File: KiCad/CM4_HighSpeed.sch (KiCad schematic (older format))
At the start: 6 parts

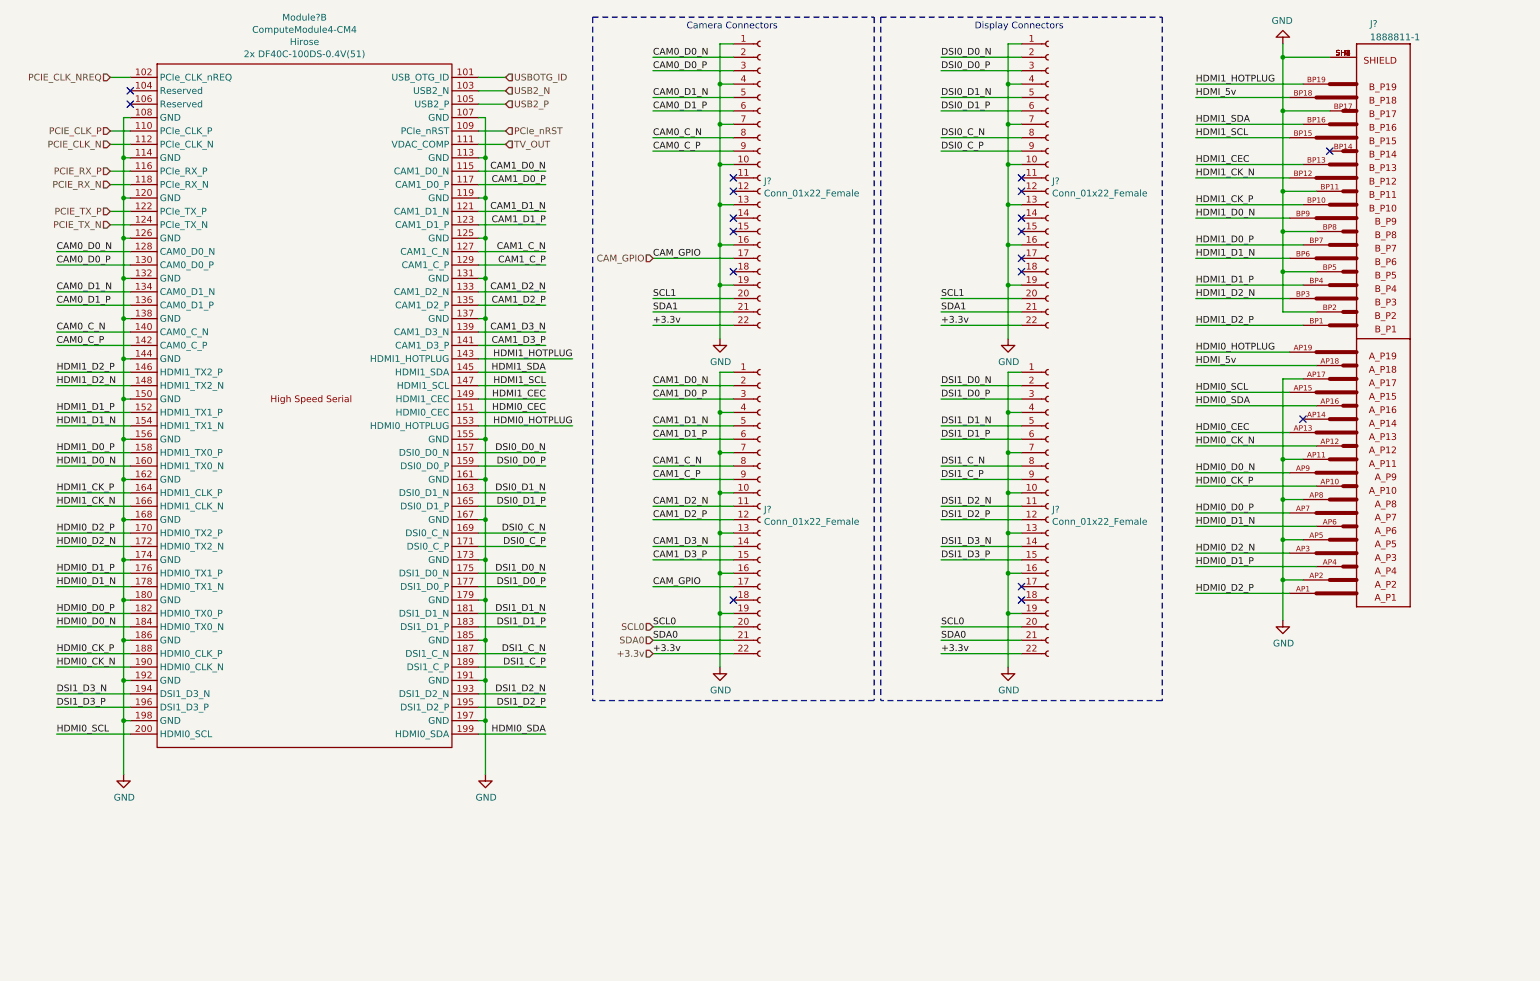
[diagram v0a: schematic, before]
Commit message: Lotsa changes
Added new footprints:
PCIe x1, TO-252 tab, SOT95, SOP50, SON50, Hirose FH-12-22S, 2.54mm 2x02 and 2x05 headers
Added new models:
Hirose FH-12-22S, FSUSB42MUX, MIC2019YM6-TR, TPS6206
Re-did ATX connector symbol wiring
Begun wiring PI7C PCI-e switch
Wired USB2517 hub
Begun adding MIC2019YM6 current limiters.
Added TODO lists to each page to help new contributors
Begun placing PCB footprints and descriptors
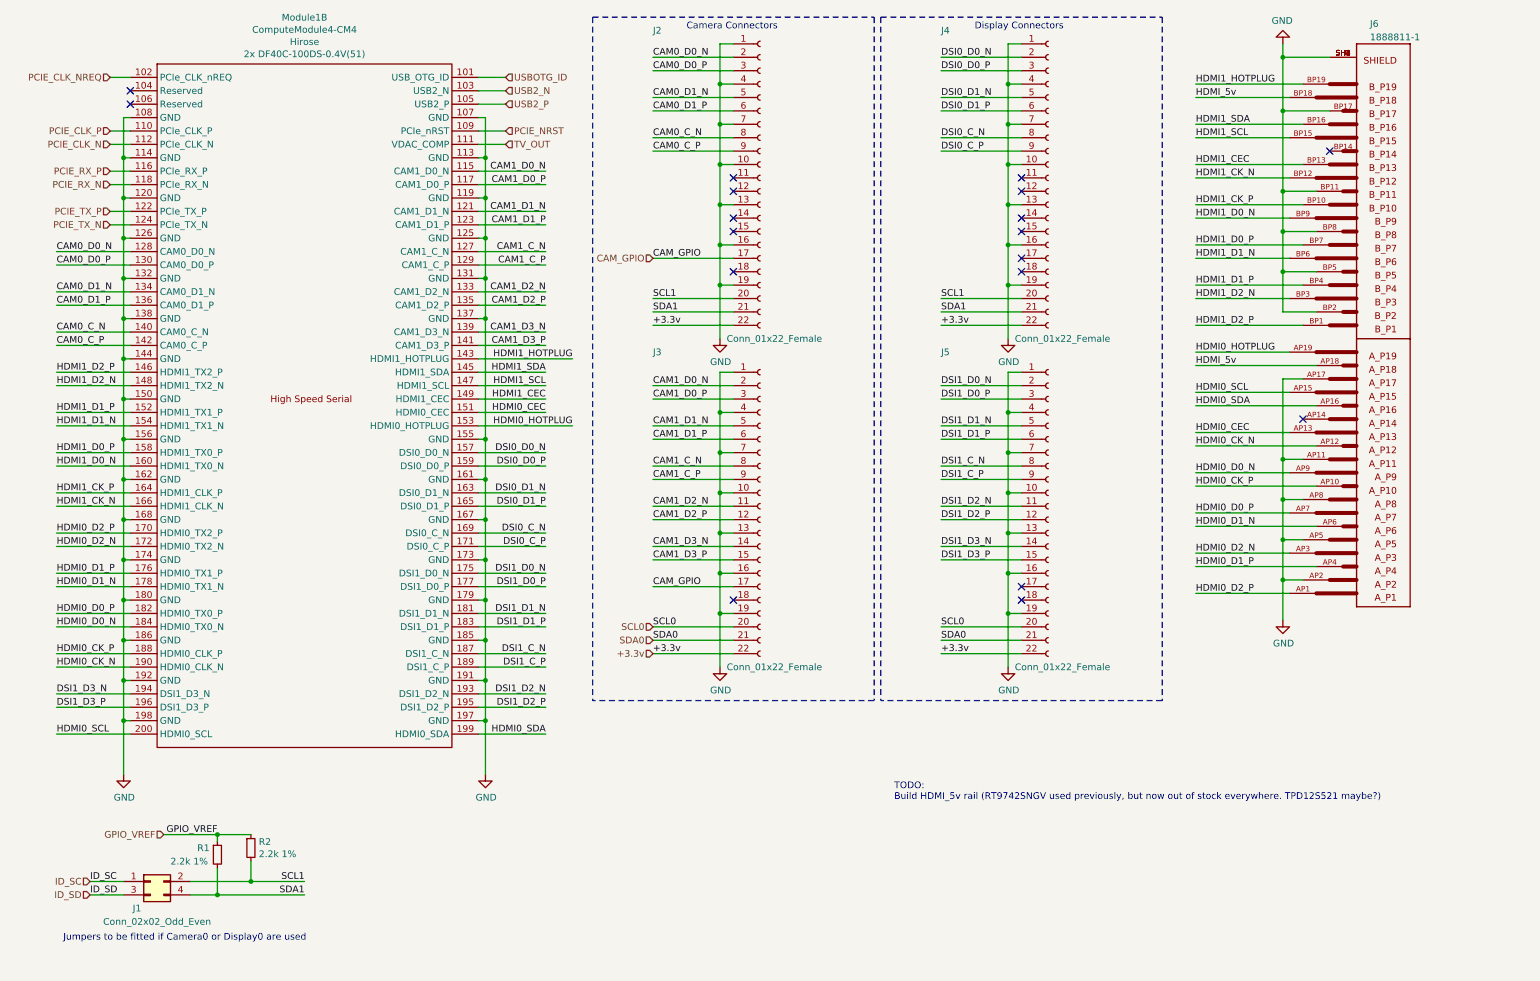
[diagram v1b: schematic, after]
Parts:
- added J1: Conn_02x02_Odd_Even, CM4_MATX:PinHeader_2x02_P2.54mm_Vertical, symbol Connector_Generic:Conn_02x02_Odd_Even
- added R1, R2: 2.2k 1%, symbol Device:R_Small
- J2, J3, J4, J5: renamed from J?; footprint (none) -> CM4_MATX:Hirose_FH12-22S-0.5SH_1x22-1MP_P0.50mm_Horizontal
- J6: renamed from J?; Manufacturer (none) -> TE Connectivity
- gave numbers to parts that had none: 1
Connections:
- net SCL1: now also J1.2 (Pin_2), R2.2
- net SDA1: now also J1.4 (Pin_4), R1.2
- net PCIe_nRST renamed PCIE_NRST
- new net GPIO_VREF: R1.1, R2.1
- new net ID_SC: J1.1 (Pin_1)
- new net ID_SD: J1.3 (Pin_3)
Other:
- note added: "Jumpers to be fitted if Camera0 or Display0 are used"
- note added: "TODO:\nBuild HDMI_5v rail (RT9742SNGV used previously, but now out of stock everywhere. TPD12S521 maybe?)\n"
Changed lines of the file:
@@
 $Descr A4 11693 8268
 encoding utf-8
-Sheet 4 5
+Sheet 2 6
 Title "CM4_MATX: CM4 High Speed IO"
 Date "2020-11-19"
@@
 	1250 1400 1250 1700
 $Comp
-L power:GND #PWR?
+L power:GND #PWR0101
 U 1 1 5FB85B54
 P 1250 6300
-F 0 "#PWR?" H 1250 6050 50  0001 C CNN
+F 0 "#PWR0101" H 1250 6050 50  0001 C CNN
 F 1 "GND" H 1255 6127 50  0000 C CNN
 F 2 "" H 1250 6300 50  0001 C CNN
@@
 	3950 1400 3950 1700
 $Comp
-L power:GND #PWR?
+L power:GND #PWR0102
 U 1 1 5FB8BA74
 P 3950 6300
-F 0 "#PWR?" H 3950 6050 50  0001 C CNN
+F 0 "#PWR0102" H 3950 6050 50  0001 C CNN
 F 1 "GND" H 3955 6127 50  0000 C CNN
 F 2 "" H 3950 6300 50  0001 C CNN
@@
 	1150 1100 1300 1100
 $Comp
-L CM4_MATX:ComputeModule4-CM4 Module?
+L CM4_MATX:ComputeModule4-CM4 Module1
 U 2 1 5FB73006
 P 350 950
-F 0 "Module?" H 2600 1247 50  0000 C CNN
+F 0 "Module1" H 2600 1247 50  0000 C CNN
 F 1 "ComputeModule4-CM4" H 2600 1156 50  0000 C CNN
 F 2 "CM4_MATX:rpiCM4" H -1250 800 50  0001 C CNN
@@
 TV_OUT
 Text HLabel 4100 1500 2    50   Input ~ 0
-PCIe_nRST
+PCIE_NRST
 Text HLabel 4100 1300 2    50   Input ~ 0
 USB2_P
@@
 	1300 1500 1150 1500
 $Comp
-L Connector:Conn_01x22_Female J?
+L Connector:Conn_01x22_Female J2
 U 1 1 5FC93FB2
 P 6000 1850
-F 0 "J?" H 6028 1826 50  0000 L CNN
-F 1 "Conn_01x22_Female" H 6028 1735 50  0000 L CNN
-F 2 "" H 6000 1850 50  0001 C CNN
+F 0 "J2" H 5200 2950 50  0000 L CNN
+F 1 "Conn_01x22_Female" H 5750 650 50  0000 L CNN
+F 2 "CM4_MATX:Hirose_FH12-22S-0.5SH_1x22-1MP_P0.50mm_Horizontal" H 6000 1850 50  0001 C CNN
 F 3 "~" H 6000 1850 50  0001 C CNN
 	1    6000 1850
@@
 $EndComp
 $Comp
-L Connector:Conn_01x22_Female J?
+L Connector:Conn_01x22_Female J3
 U 1 1 5FC97DA8
 P 6000 4300
-F 0 "J?" H 6028 4276 50  0000 L CNN
-F 1 "Conn_01x22_Female" H 6028 4185 50  0000 L CNN
-F 2 "" H 6000 4300 50  0001 C CNN
+F 0 "J3" H 5200 5450 50  0000 L CNN
+F 1 "Conn_01x22_Female" H 5750 3100 50  0000 L CNN
+F 2 "CM4_MATX:Hirose_FH12-22S-0.5SH_1x22-1MP_P0.50mm_Horizontal" H 6000 4300 50  0001 C CNN
 F 3 "~" H 6000 4300 50  0001 C CNN
 	1    6000 4300
@@
 $EndComp
 $Comp
-L power:GND #PWR?
+L power:GND #PWR0103
 U 1 1 5FCA1944
 P 5700 3050
-F 0 "#PWR?" H 5700 2800 50  0001 C CNN
+F 0 "#PWR0103" H 5700 2800 50  0001 C CNN
 F 1 "GND" H 5705 2877 50  0000 C CNN
 F 2 "" H 5700 3050 50  0001 C CNN
@@
 	5700 3300 5700 3600
 $Comp
-L power:GND #PWR?
+L power:GND #PWR0104
 U 1 1 5FD6AAE5
 P 5700 5500
-F 0 "#PWR?" H 5700 5250 50  0001 C CNN
+F 0 "#PWR0104" H 5700 5250 50  0001 C CNN
 F 1 "GND" H 5705 5327 50  0000 C CNN
 F 2 "" H 5700 5500 50  0001 C CNN
@@
 Camera Connectors
 $Comp
-L Connector:Conn_01x22_Female J?
+L Connector:Conn_01x22_Female J4
 U 1 1 5FE5DC13
 P 8150 1850
-F 0 "J?" H 8178 1826 50  0000 L CNN
-F 1 "Conn_01x22_Female" H 8178 1735 50  0000 L CNN
-F 2 "" H 8150 1850 50  0001 C CNN
+F 0 "J4" H 7350 2950 50  0000 L CNN
+F 1 "Conn_01x22_Female" H 7900 650 50  0000 L CNN
+F 2 "CM4_MATX:Hirose_FH12-22S-0.5SH_1x22-1MP_P0.50mm_Horizontal" H 8150 1850 50  0001 C CNN
 F 3 "~" H 8150 1850 50  0001 C CNN
 	1    8150 1850
@@
 $EndComp
 $Comp
-L Connector:Conn_01x22_Female J?
+L Connector:Conn_01x22_Female J5
 U 1 1 5FE5DC19
 P 8150 4300
-F 0 "J?" H 8178 4276 50  0000 L CNN
-F 1 "Conn_01x22_Female" H 8178 4185 50  0000 L CNN
-F 2 "" H 8150 4300 50  0001 C CNN
+F 0 "J5" H 7350 5450 50  0000 L CNN
+F 1 "Conn_01x22_Female" H 7900 3100 50  0000 L CNN
+F 2 "CM4_MATX:Hirose_FH12-22S-0.5SH_1x22-1MP_P0.50mm_Horizontal" H 8150 4300 50  0001 C CNN
 F 3 "~" H 8150 4300 50  0001 C CNN
 	1    8150 4300
@@
 $EndComp
 $Comp
-L power:GND #PWR?
+L power:GND #PWR0105
 U 1 1 5FE5DC1F
 P 7850 3050
-F 0 "#PWR?" H 7850 2800 50  0001 C CNN
+F 0 "#PWR0105" H 7850 2800 50  0001 C CNN
 F 1 "GND" H 7855 2877 50  0000 C CNN
 F 2 "" H 7850 3050 50  0001 C CNN
@@
 	7850 3300 7850 3600
 $Comp
-L power:GND #PWR?
+L power:GND #PWR0106
 U 1 1 5FE5DC55
 P 7850 5500
-F 0 "#PWR?" H 7850 5250 50  0001 C CNN
+F 0 "#PWR0106" H 7850 5250 50  0001 C CNN
 F 1 "GND" H 7855 5327 50  0000 C CNN
 F 2 "" H 7850 5500 50  0001 C CNN
@@
 NoConn ~ 7950 4900
 $Comp
-L CM4_MATX:1888811-1 J?
+L CM4_MATX:1888811-1 J6
 U 1 1 5FEABA7A
 P 10450 3050
-F 0 "J?" H 10350 700 50  0000 R CNN
+F 0 "J6" H 10350 700 50  0000 R CNN
 F 1 "1888811-1" H 10350 800 50  0000 R CNN
 F 2 "TE_1888811-1" H 10450 3050 50  0001 L BNN
@@
 F 5 "A1" H 10450 3050 50  0001 L BNN "PARTREV"
 F 6 "Manufacturer Recommendations" H 10450 3050 50  0001 L BNN "STANDARD"
+F 7 "TE Connectivity" H 10450 3050 50  0001 C CNN "Manufacturer"
 	1    10450 3050
 	-1   0    0    1
@@
 	9900 2850 9900 2550
 $Comp
-L power:GND #PWR?
+L power:GND #PWR0107
 U 1 1 5FEBFD17
 P 9900 850
-F 0 "#PWR?" H 9900 600 50  0001 C CNN
+F 0 "#PWR0107" H 9900 600 50  0001 C CNN
 F 1 "GND" H 9905 677 50  0000 C CNN
 F 2 "" H 9900 850 50  0001 C CNN
@@
 	9900 3350 9900 3950
 $Comp
-L power:GND #PWR?
+L power:GND #PWR0108
 U 1 1 6008E7C2
 P 9900 5150
-F 0 "#PWR?" H 9900 4900 50  0001 C CNN
+F 0 "#PWR0108" H 9900 4900 50  0001 C CNN
 F 1 "GND" H 9905 4977 50  0000 C CNN
 F 2 "" H 9900 5150 50  0001 C CNN
@@
 Wire Wire Line
 	9250 1150 10050 1150
+Text Notes 7000 6500 0    50   ~ 0
+TODO:\nBuild HDMI_5v rail (RT9742SNGV used previously, but now out of stock everywhere. TPD12S521 maybe?)\n
+Text HLabel 1550 6750 0    50   Input ~ 0
+GPIO_VREF
+$Comp
+L Device:R_Small R1
+U 1 1 5FD49D55
+P 1950 6900
+F 0 "R1" H 1800 6950 50  0000 L CNN
+F 1 "2.2k 1%" H 1600 6850 50  0000 L CNN
+F 2 "" H 1950 6900 50  0001 C CNN
+F 3 "~" H 1950 6900 50  0001 C CNN
+	1    1950 6900
+	1    0    0    -1
+$EndComp
+$Comp
+L Device:R_Small R2
+U 1 1 5FD4A3BC
+P 2200 6850
+F 0 "R2" H 2259 6896 50  0000 L CNN
+F 1 "2.2k 1%" H 2259 6805 50  0000 L CNN
+F 2 "" H 2200 6850 50  0001 C CNN
+F 3 "~" H 2200 6850 50  0001 C CNN
+	1    2200 6850
+	1    0    0    -1
+$EndComp
+Text Label 1950 6750 2    50   ~ 0
+GPIO_VREF
+Connection ~ 1950 6750
+Wire Wire Line
+	1950 6750 2200 6750
+Wire Wire Line
+	1550 6750 1950 6750
+$Comp
+L Connector_Generic:Conn_02x02_Odd_Even J1
+U 1 1 5FD77353
+P 1450 7100
+F 0 "J1" H 1350 6900 50  0000 C CNN
+F 1 "Conn_02x02_Odd_Even" H 1500 6800 50  0000 C CNN
+F 2 "CM4_MATX:PinHeader_2x02_P2.54mm_Vertical" H 1450 7100 50  0001 C CNN
+F 3 "~" H 1450 7100 50  0001 C CNN
+	1    1450 7100
+	1    0    0    -1
+$EndComp
+Text HLabel 1000 7100 0    50   Input ~ 0
+ID_SC
+Text HLabel 1000 7200 0    50   Input ~ 0
+ID_SD
+Text Label 1000 7100 0    50   ~ 0
+ID_SC
+Text Label 1000 7200 0    50   ~ 0
+ID_SD
+Wire Wire Line
+	1000 7200 1250 7200
+Wire Wire Line
+	1250 7100 1000 7100
+Text Label 2600 7100 2    50   ~ 0
+SCL1
+Text Label 2600 7200 2    50   ~ 0
+SDA1
+Wire Wire Line
+	1750 7100 2200 7100
+Wire Wire Line
+	2200 7100 2200 6950
+Connection ~ 2200 7100
+Wire Wire Line
+	2200 7100 2600 7100
+Text Notes 800  7550 0    50   ~ 0
+Jumpers to be fitted if Camera0 or Display0 are used
+Wire Wire Line
+	1950 6750 1950 6800
+Wire Wire Line
+	1750 7200 1950 7200
+Wire Wire Line
+	1950 7000 1950 7200
+Connection ~ 1950 7200
+Wire Wire Line
+	1950 7200 2600 7200
 $EndSCHEMATC

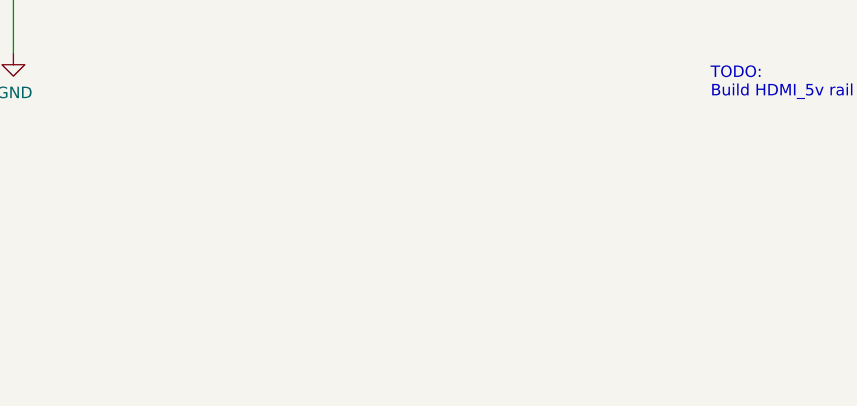
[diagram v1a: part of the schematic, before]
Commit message: Many, many changes...
Added a bunch of new footprints and a couple of new symbols.
Added the other side of the CM4 connector and wired its features.
Added some more detailed models for a fair few components.
Added a new schematic to handle power for USB ports.
Updated the PCB with the new components and moved some around to populate the rear IO panel.
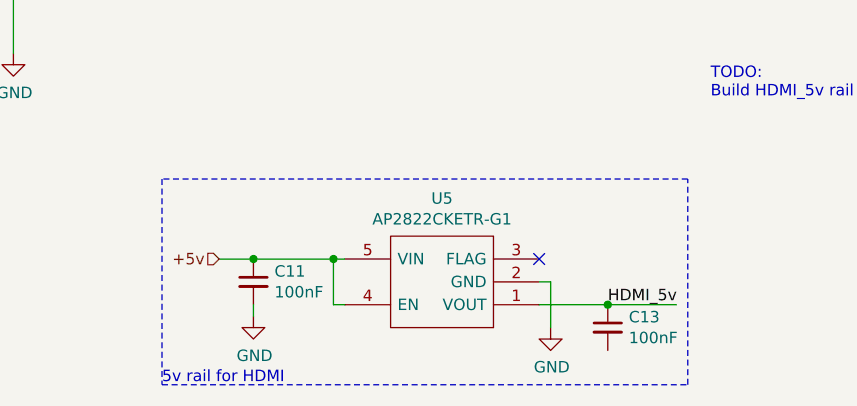
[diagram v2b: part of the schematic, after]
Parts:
- added C11, C13: 100nF, symbol Device:C_Small
- added U5: AP2822CKETR-G1, CM4_MATX:SOT95P282X145-5N, symbol CM4_MATX:AP2822CKETR-G1
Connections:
- net GND: now also C11.2, U5.2 (GND)
- net HDMI_5v: now also C13.1, U5.1 (VOUT)
- new net +5v: C11.1, U5.4 (EN), U5.5 (VIN)
- no-connect marks 18 -> 19
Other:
- note added: "5v rail for HDMI"
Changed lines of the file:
@@
 $Descr A4 11693 8268
 encoding utf-8
-Sheet 2 6
+Sheet 2 8
 Title "CM4_MATX: CM4 High Speed IO"
 Date "2020-11-19"
@@
 Wire Wire Line
 	1950 7200 2600 7200
+$Comp
+L CM4_MATX:AP2822CKETR-G1 U5
+U 1 1 606F7FB7
+P 6250 7400
+F 0 "U5" H 6675 6935 50  0000 C CNN
+F 1 "AP2822CKETR-G1" H 6675 7026 50  0000 C CNN
+F 2 "CM4_MATX:SOT95P282X145-5N" H 7200 7500 50  0001 L CNN
+F 3 "https://www.diodes.com/assets/Datasheets/products_inactive_data/AP2822.pdf" H 7200 7400 50  0001 L CNN
+F 4 "Power Switch/Driver 1:1 N-Channel 1A SOT-23-5" H 7200 7300 50  0001 L CNN "Description"
+F 5 "1.45" H 7200 7200 50  0001 L CNN "Height"
+F 6 "621-AP2822CKETR-G1" H 7200 7100 50  0001 L CNN "Mouser Part Number"
+F 7 "https://www.mouser.co.uk/ProductDetail/Diodes-Incorporated/AP2822CKETR-G1?qs=5V6w%252Be2aIqZGZGFGIHi7bg%3D%3D" H 7200 7000 50  0001 L CNN "Mouser Price/Stock"
+F 8 "Diodes Inc." H 7200 6900 50  0001 L CNN "Manufacturer_Name"
+F 9 "AP2822CKETR-G1" H 7200 6800 50  0001 L CNN "Manufacturer_Part_Number"
+	1    6250 7400
+	-1   0    0    1
+$EndComp
+$Comp
+L Device:C_Small C13
+U 1 1 607440BA
+P 6550 7500
+F 0 "C13" H 6642 7546 50  0000 L CNN
+F 1 "100nF" H 6642 7455 50  0000 L CNN
+F 2 "" H 6550 7500 50  0001 C CNN
+F 3 "~" H 6550 7500 50  0001 C CNN
+	1    6550 7500
+	1    0    0    -1
+$EndComp
+Wire Wire Line
+	6250 7400 6550 7400
+Text Label 6550 7400 0    50   ~ 0
+HDMI_5v
+Wire Wire Line
+	6550 7400 6850 7400
+Connection ~ 6550 7400
+Wire Wire Line
+	6250 7300 6300 7300
+Wire Wire Line
+	6300 7300 6300 7500
+$Comp
+L power:GND #PWR0138
+U 1 1 6078E634
+P 6300 7500
+F 0 "#PWR0138" H 6300 7250 50  0001 C CNN
+F 1 "GND" H 6305 7327 50  0000 C CNN
+F 2 "" H 6300 7500 50  0001 C CNN
+F 3 "" H 6300 7500 50  0001 C CNN
+	1    6300 7500
+	1    0    0    -1
+$EndComp
+NoConn ~ 6250 7200
+Text HLabel 4850 7200 0    50   Input ~ 0
++5v
+$Comp
+L Device:C_Small C11
+U 1 1 607D8C18
+P 5000 7300
+F 0 "C11" H 5092 7346 50  0000 L CNN
+F 1 "100nF" H 5092 7255 50  0000 L CNN
+F 2 "" H 5000 7300 50  0001 C CNN
+F 3 "~" H 5000 7300 50  0001 C CNN
+	1    5000 7300
+	1    0    0    -1
+$EndComp
+Wire Wire Line
+	5000 7200 4850 7200
+Wire Wire Line
+	5000 7200 5350 7200
+Connection ~ 5000 7200
+$Comp
+L power:GND #PWR0153
+U 1 1 6080BEE5
+P 5000 7450
+F 0 "#PWR0153" H 5000 7200 50  0001 C CNN
+F 1 "GND" H 5005 7277 50  0000 C CNN
+F 2 "" H 5000 7450 50  0001 C CNN
+F 3 "" H 5000 7450 50  0001 C CNN
+	1    5000 7450
+	1    0    0    -1
+$EndComp
+Wire Wire Line
+	5000 7450 5000 7400
+Wire Wire Line
+	5350 7200 5350 7400
+Wire Wire Line
+	5350 7400 5400 7400
+Connection ~ 5350 7200
+Wire Wire Line
+	5350 7200 5400 7200
+Wire Notes Line
+	4600 7750 6900 7750
+Wire Notes Line
+	6900 7750 6900 6850
+Wire Notes Line
+	6900 6850 4600 6850
+Wire Notes Line
+	4600 6850 4600 7750
+Text Notes 4600 7750 0    50   ~ 0
+5v rail for HDMI
 $EndSCHEMATC

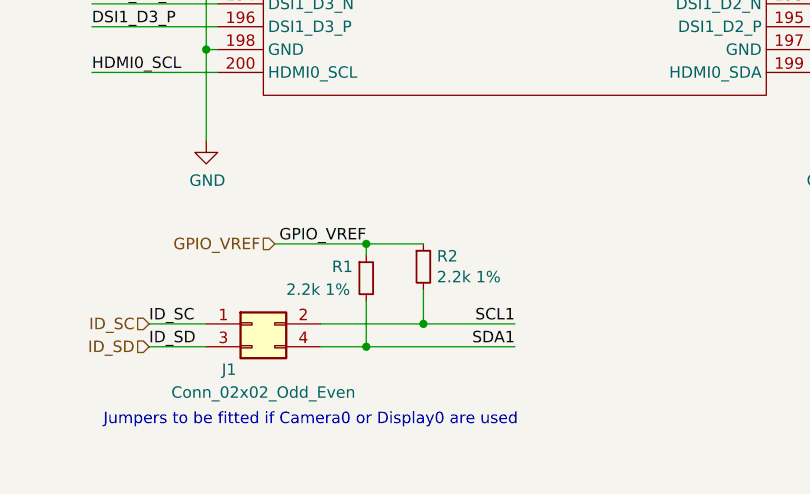
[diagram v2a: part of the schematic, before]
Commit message: Small changes to PCIe, USB Schematics and board layout, legend for GPIO pins.
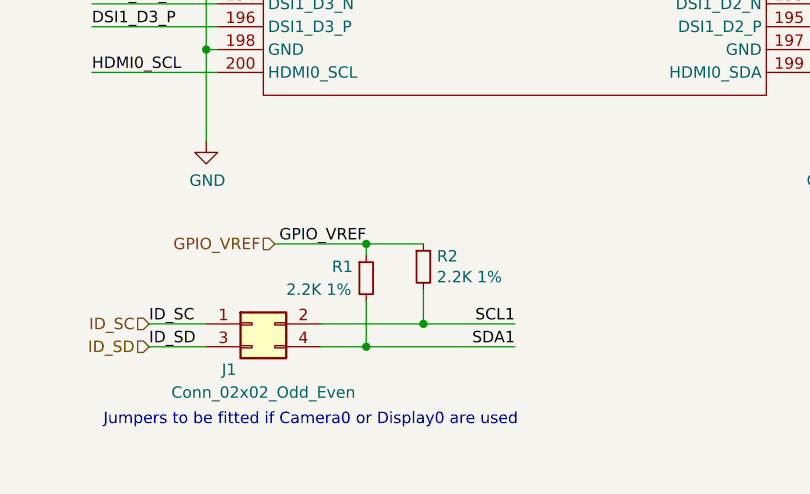
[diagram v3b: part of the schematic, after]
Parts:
- R1, R2: value 2.2k 1% -> 2.2K 1%
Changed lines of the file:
@@
 $Descr A4 11693 8268
 encoding utf-8
-Sheet 2 8
+Sheet 2 10
 Title "CM4_MATX: CM4 High Speed IO"
-Date "2020-11-19"
+Date "2020-11-27"
 Rev "0.1"
-Comp "Oliver Møller/TheGuyDanish"
+Comp "CM4_MATX Contributors"
 Comment1 "https://github.com/theguydanish/CM4_MATX"
 Comment2 ""
@@
 P 1950 6900
 F 0 "R1" H 1800 6950 50  0000 L CNN
-F 1 "2.2k 1%" H 1600 6850 50  0000 L CNN
+F 1 "2.2K 1%" H 1600 6850 50  0000 L CNN
 F 2 "" H 1950 6900 50  0001 C CNN
 F 3 "~" H 1950 6900 50  0001 C CNN
@@
 P 2200 6850
 F 0 "R2" H 2259 6896 50  0000 L CNN
-F 1 "2.2k 1%" H 2259 6805 50  0000 L CNN
+F 1 "2.2K 1%" H 2259 6805 50  0000 L CNN
 F 2 "" H 2200 6850 50  0001 C CNN
 F 3 "~" H 2200 6850 50  0001 C CNN

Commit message: Updating PCIe symbols + PCIe power stub sheet
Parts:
- J6: footprint TE_1888811-1 -> CM4_MATX:TE_1888811-1
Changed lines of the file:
@@
 $Descr A4 11693 8268
 encoding utf-8
-Sheet 2 10
+Sheet 2 11
 Title "CM4_MATX: CM4 High Speed IO"
 Date "2020-12-14"
@@
 F 0 "J6" H 10350 700 50  0000 R CNN
 F 1 "1888811-1" H 10350 800 50  0000 R CNN
-F 2 "TE_1888811-1" H 10450 3050 50  0001 L BNN
+F 2 "CM4_MATX:TE_1888811-1" H 10450 3050 50  0001 L BNN
 F 3 "" H 10450 3050 50  0001 L BNN
 F 4 "TE CONNECTIVITY" H 10450 3050 50  0001 L BNN "MANUFACTURER"
